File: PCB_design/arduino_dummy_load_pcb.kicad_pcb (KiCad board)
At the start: 2 copper layers, 209.6 x 109.2 mm, 114 parts, among them J1 Barrel_Jack, J2 Conn_02x08_Odd_Even, U1 MCP3208

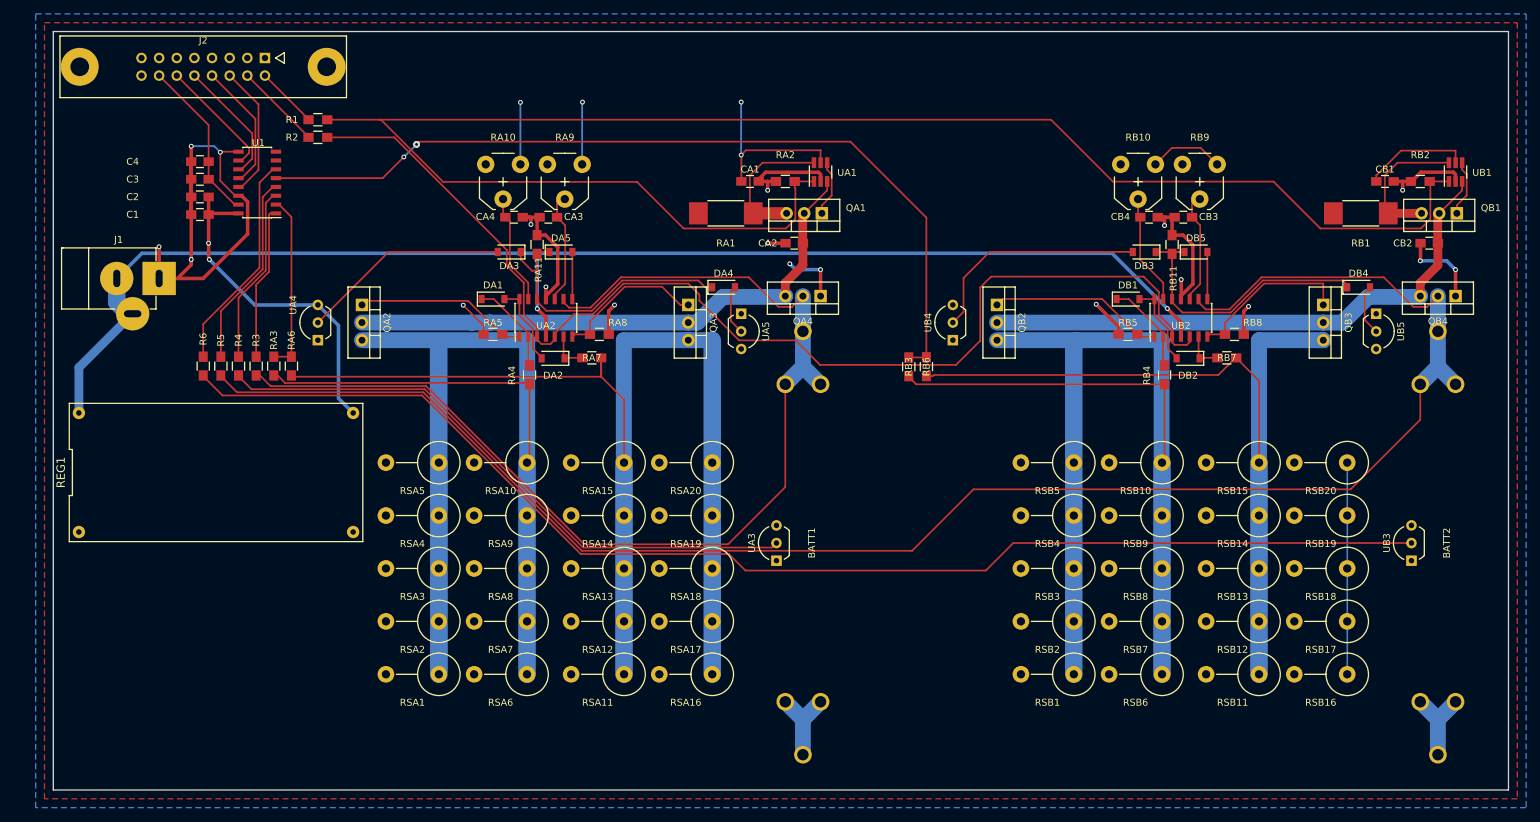
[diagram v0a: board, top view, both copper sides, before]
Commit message: Fixed apparent Kicad DRC errors (VCC floodfill in some areas was isolated from VCC.) and one via that was too close to a track, and deleted some garbage traces
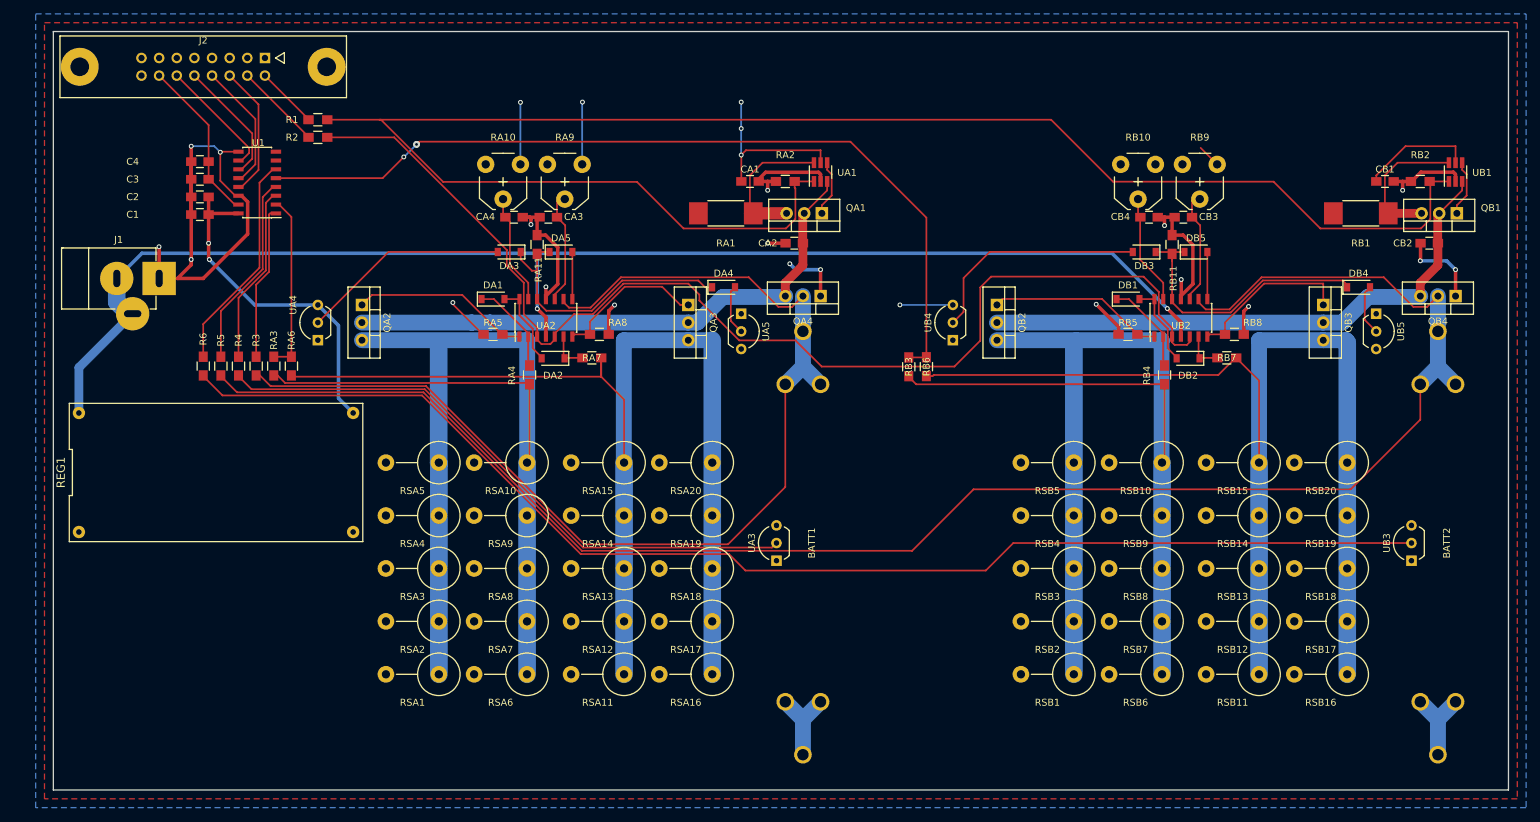
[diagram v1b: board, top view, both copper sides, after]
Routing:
- net Net-(QB3-Pad3): track 180.8 -> 232.8 mm
- net GND: track 202.4 -> 203.4 mm
- net +5V: track 118.6 -> 119.7 mm, vias 6 -> 8
- net Net-(QA2-Pad1): track 25.3 -> 26.0 mm

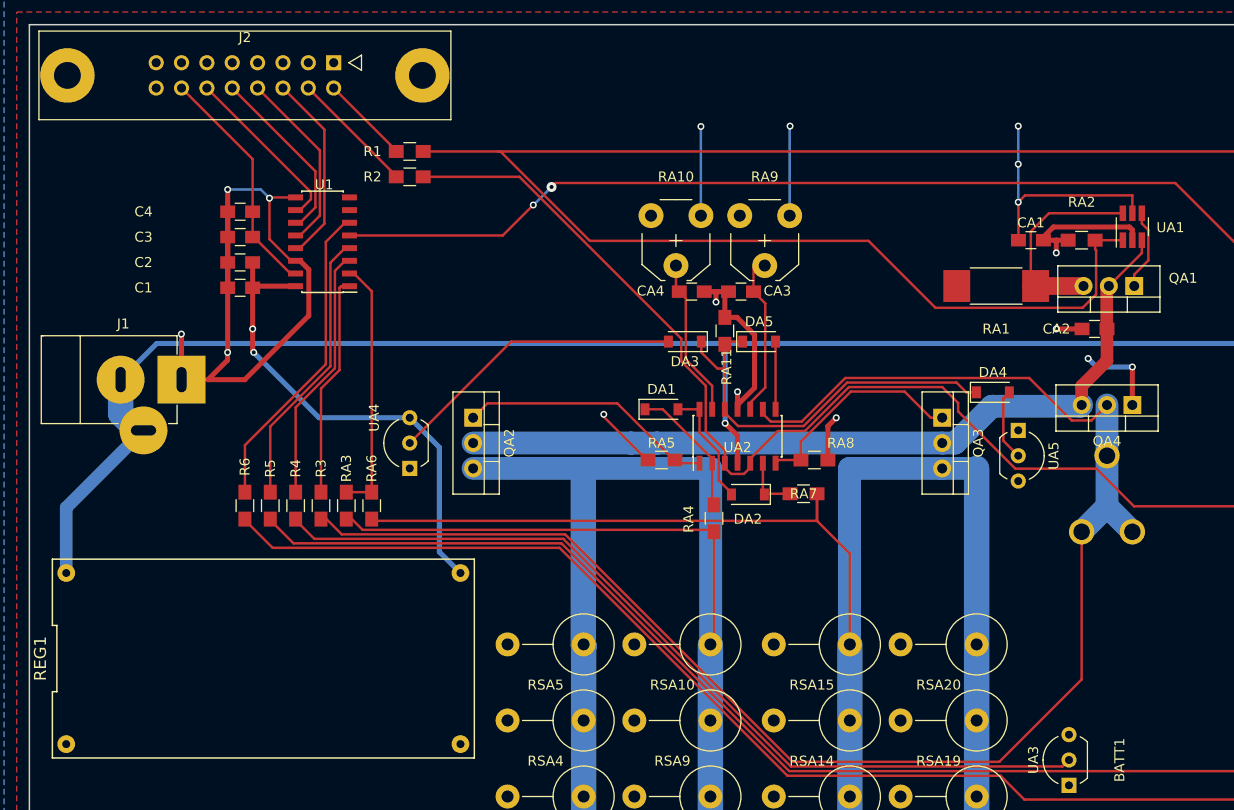
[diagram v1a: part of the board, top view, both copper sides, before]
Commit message: added readme (needs lots of work), basically final PCB
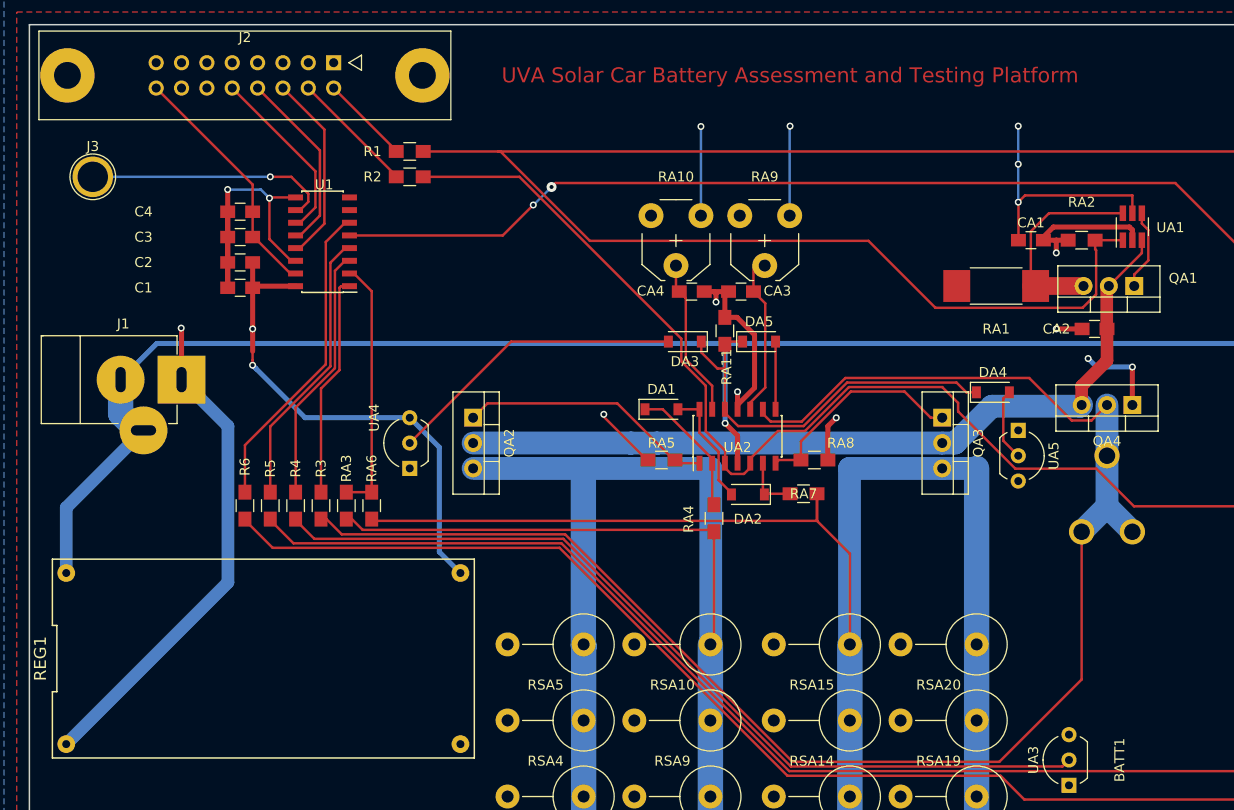
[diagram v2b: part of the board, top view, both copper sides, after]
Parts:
- added J3: Conn_01x01, Connectors:1pin, F.Cu at (62.2, 53.3)
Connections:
- J1 pad 1: GND -> Net-(J1-Pad1)
- J2 pad 14: VREF -> Net-(J2-Pad14)
- J2 pad 16: Net-(J2-Pad16) -> VREF
- REG1 pad 2: GND -> Net-(J1-Pad1)
- U1 pad 10: Net-(J2-Pad12) -> Net-(J3-Pad1)
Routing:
- net Net-(J1-Pad1): track 0.00 -> 50.3 mm, vias 0 -> 1
- net GND: track 203.4 -> 167.6 mm, vias 19 -> 17
- net Net-(J3-Pad1): track 0.00 -> 24.7 mm, vias 0 -> 1
- net Net-(J2-Pad12): track 17.4 -> 0.00 mm
- net VREF: track 23.7 -> 24.7 mm
- net +5V: track 119.7 -> 120.5 mm
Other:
- board text added: "UVA Solar Car Battery Assessment and Testing Platform"

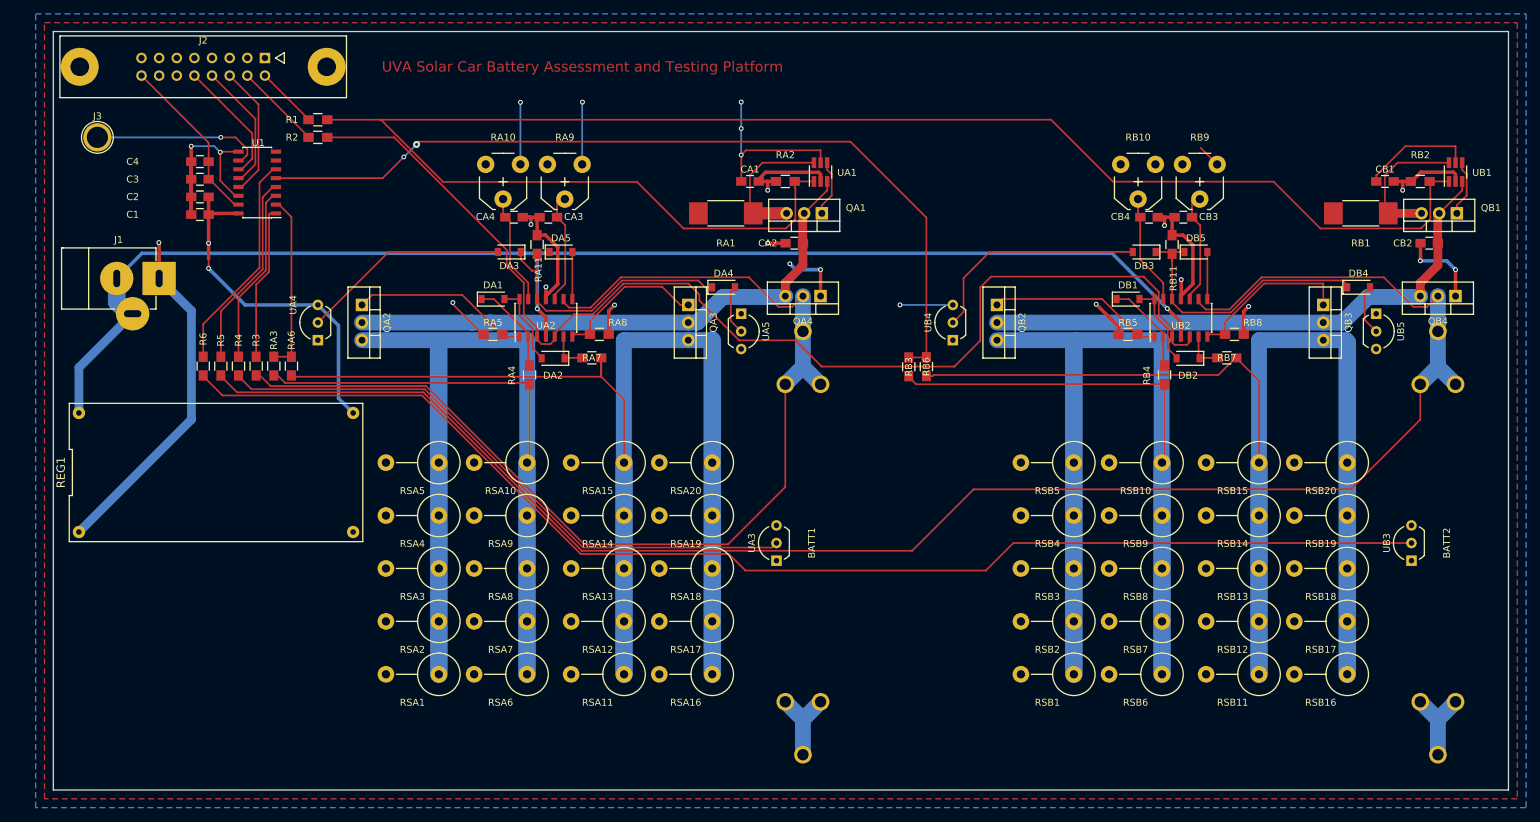
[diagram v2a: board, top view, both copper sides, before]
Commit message: Added Silkscreen Labels :)
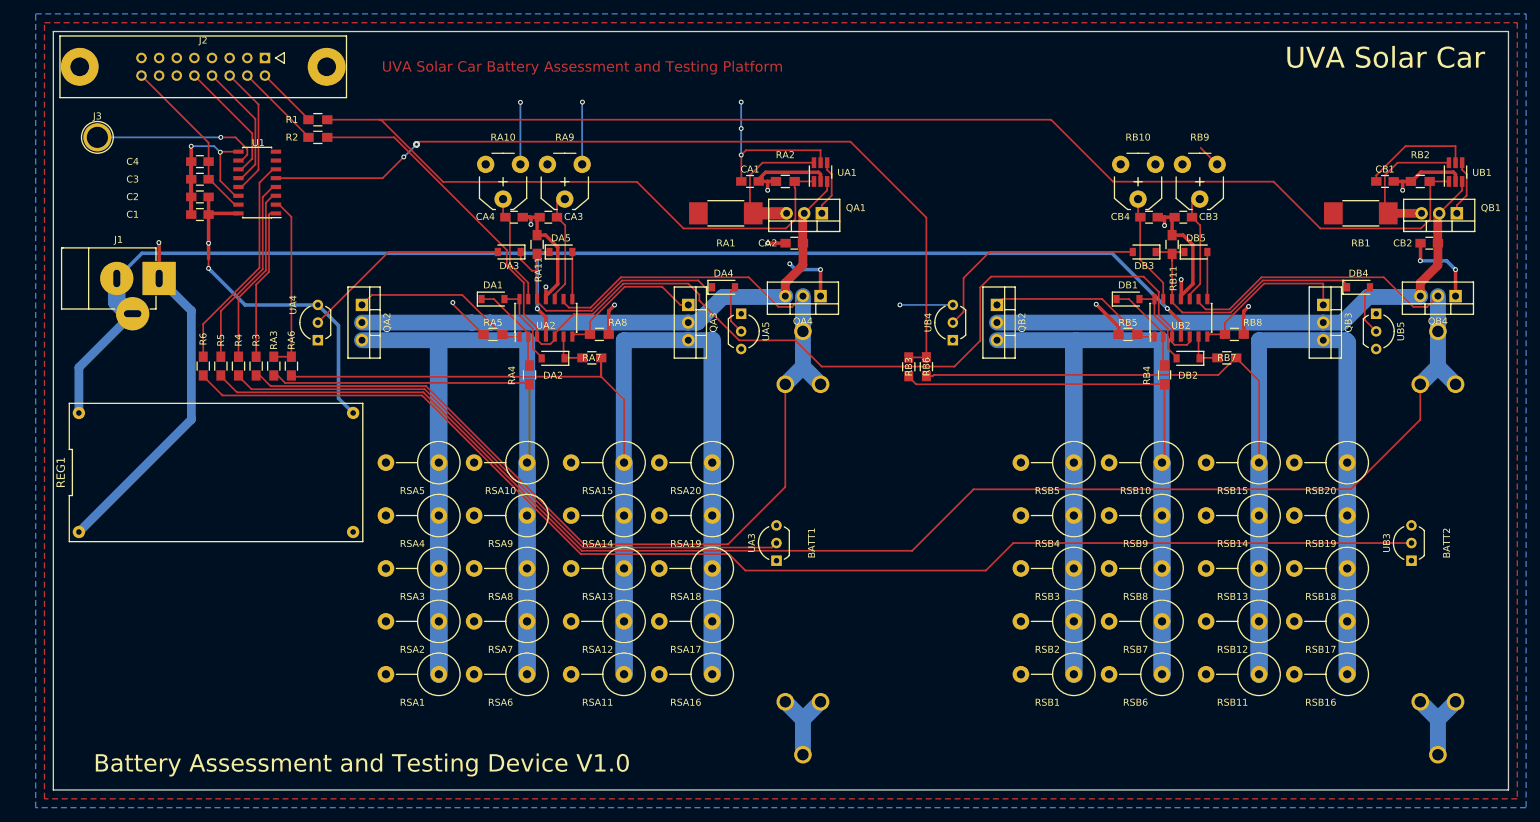
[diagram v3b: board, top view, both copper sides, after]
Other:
- board text added: "Battery Assessment and Testing Device V1.0"
- board text added: "UVA Solar Car"
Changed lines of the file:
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@@
     (area 43.914287 30.439405 267.970001 149.860001)
     (thickness 1.6)
-    (drawings 9)
+    (drawings 11)
     (tracks 609)
     (zones 0)
@@
   (page A4)
   (layers
-    (0 F.Cu signal)
+    (0 F.Cu signal hide)
     (31 B.Cu signal)
     (32 B.Adhes user)
@@
       (net 59 "Net-(J3-Pad1)"))
   )
+  (gr_text "Battery Assessment and Testing Device V1.0" (at 100.33 143.51) (layer F.SilkS)
+    (effects (font (size 2.5 2.5) (thickness 0.3)))
+  )
+  (gr_text "UVA Solar Car" (at 247.65 41.91) (layer F.SilkS)
+    (effects (font (size 3 3) (thickness 0.3)))
+  )
   (gr_text "UVA Solar Car Battery Assessment and Testing Platform" (at 132.08 43.18) (layer F.Cu)

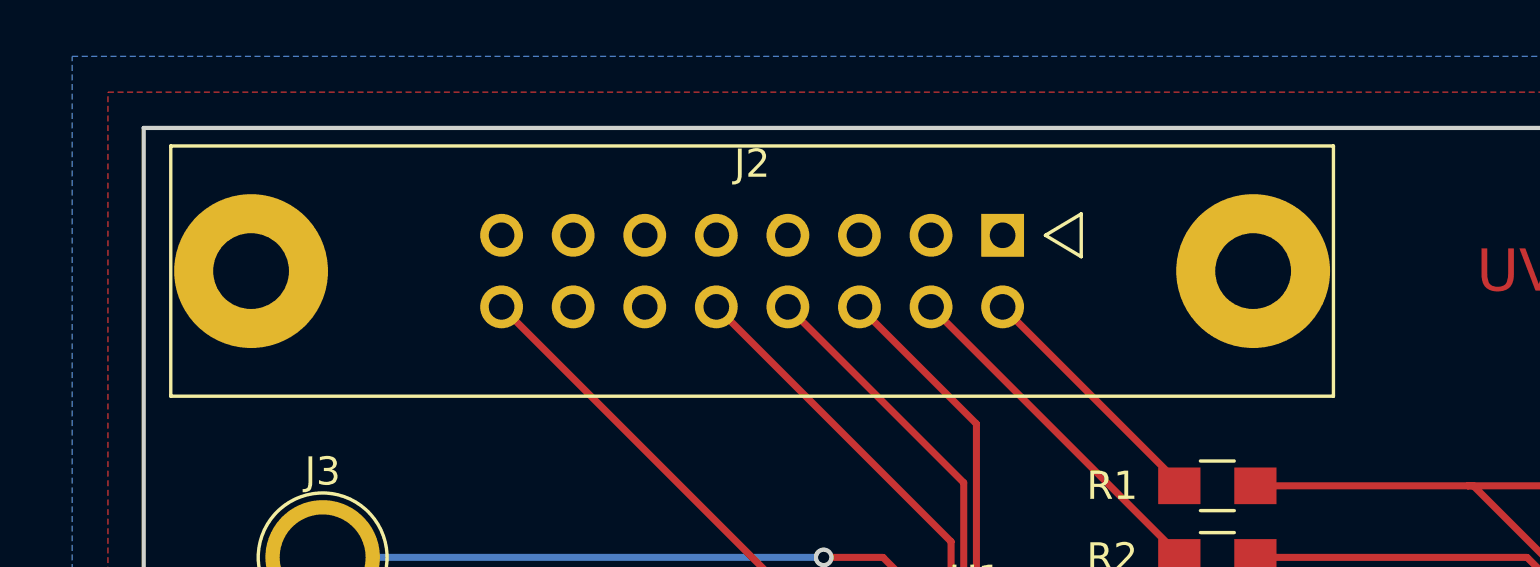
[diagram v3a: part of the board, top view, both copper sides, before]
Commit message: Moved components in the top left away from the corner...still need to adjust copper pours
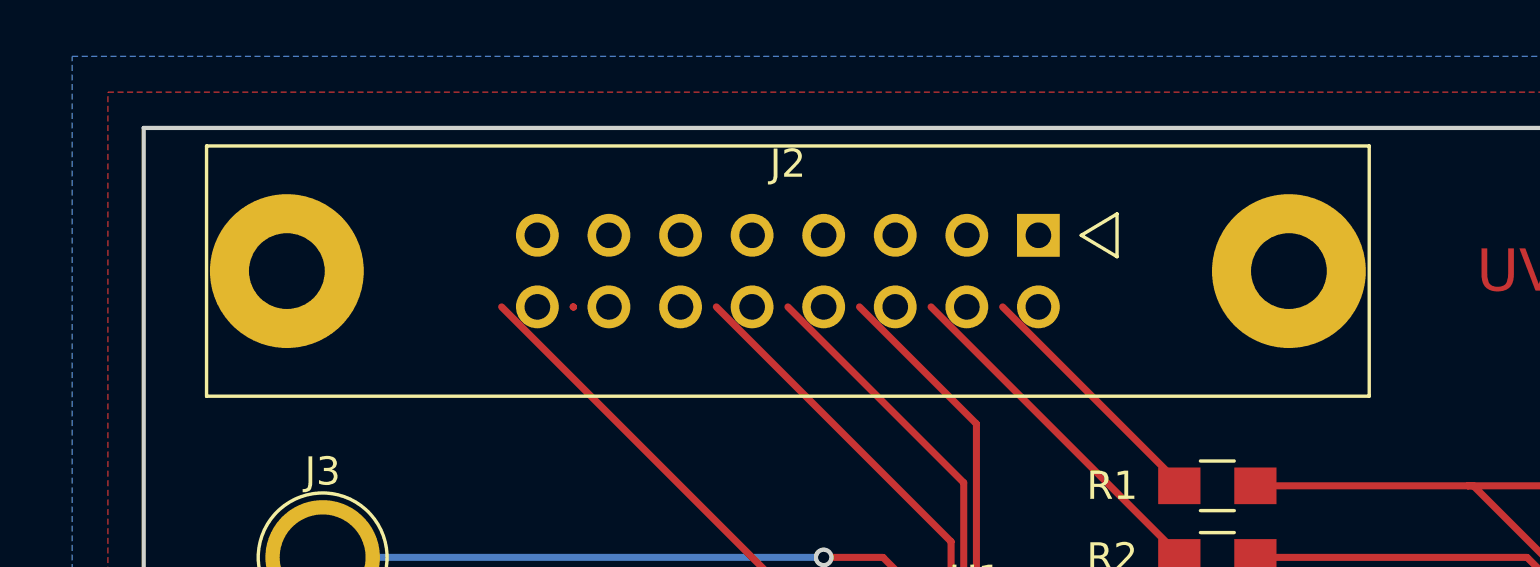
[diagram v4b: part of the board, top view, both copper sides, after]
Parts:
- moved J2 1.27 mm to (87.6, 41.9)
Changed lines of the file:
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@@
   )
   (module Connectors:he10-16d (layer F.Cu)
-    (at 86.36 41.91 180)
+    (at 87.63 41.91 180)
     (descr "Connecteur HE10 16 contacts droit")
     (tags "CONN HE10")
